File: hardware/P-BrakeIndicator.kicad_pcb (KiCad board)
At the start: 2 copper layers, 33.5 x 25.5 mm, 19 parts, among them J1 -PRW+, J2 RX TX, J3 +SPK-, Q1 2N7000, U1 ATtiny202

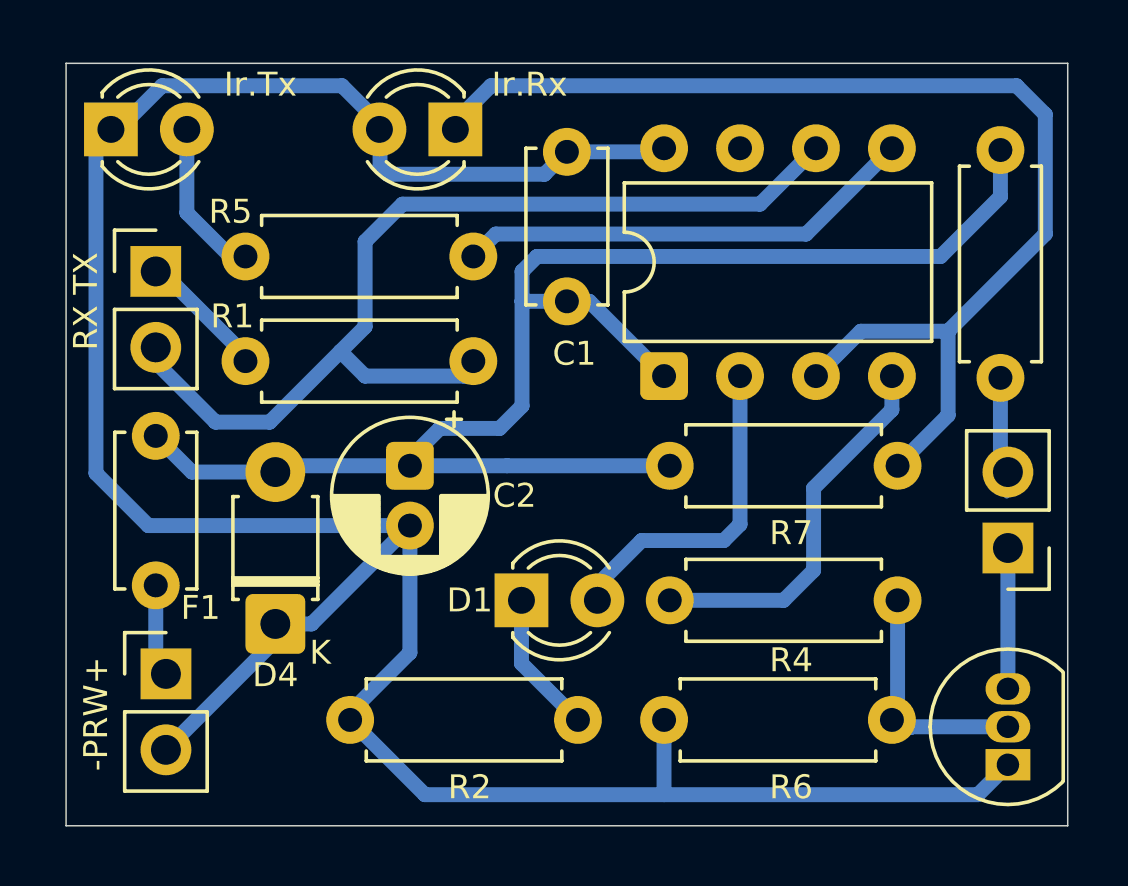
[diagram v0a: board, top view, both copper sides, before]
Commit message: pcb: Update board layout and routing
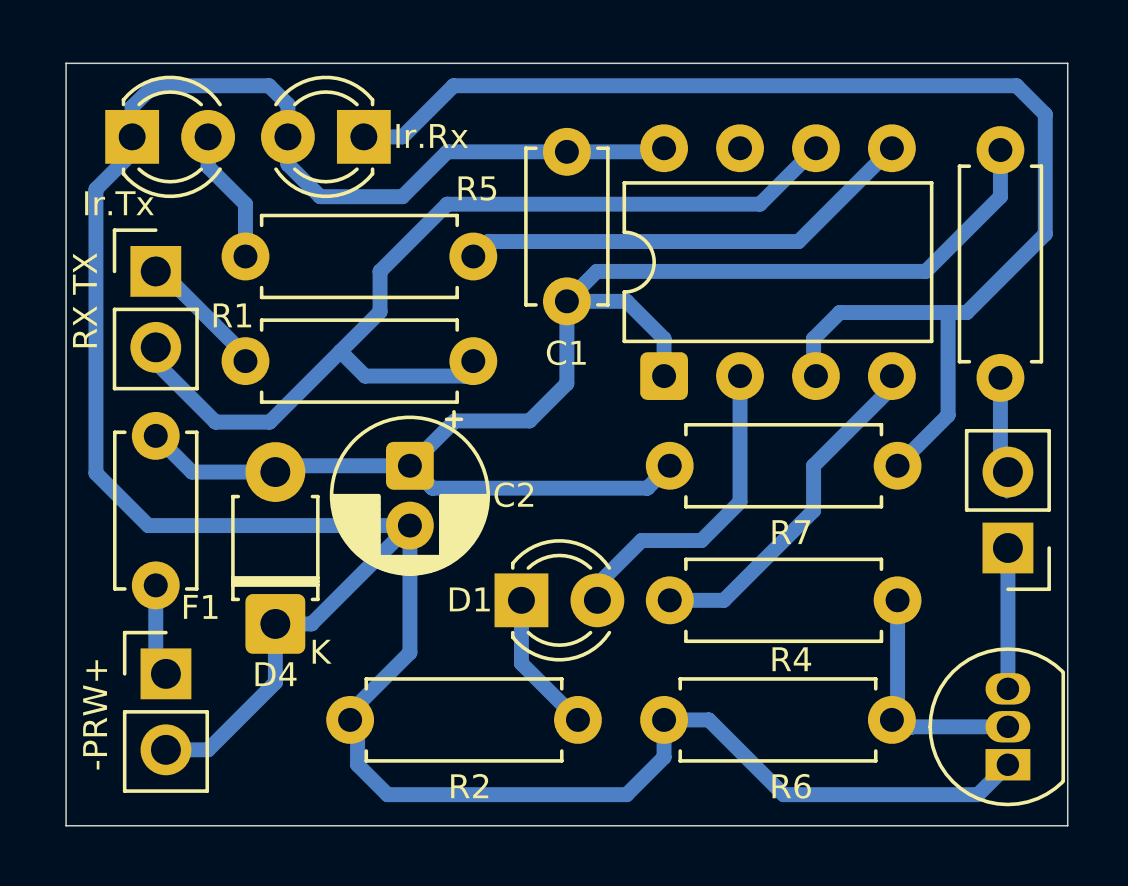
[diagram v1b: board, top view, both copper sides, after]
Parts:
- moved D3 3.07 mm to (60.0, 56.0)
- moved D2 0.75 mm to (52.2, 56.0)
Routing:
- net Net-(D3-K): track 40.2 -> 44.7 mm
- net GND: track 91.3 -> 92.8 mm
- net Net-(U1-PA1): track 13.4 -> 12.2 mm
- net Net-(D2-A): track 5.56 -> 4.52 mm
- net Net-(J2-Pin_2): track 33.5 -> 32.6 mm
- net Net-(D4-A2): track 52.5 -> 51.8 mm
